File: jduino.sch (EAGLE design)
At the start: 20 parts, among them IC1 7805T, IC2 ATMEGA48/88/168-PU, Q1 16 mHz

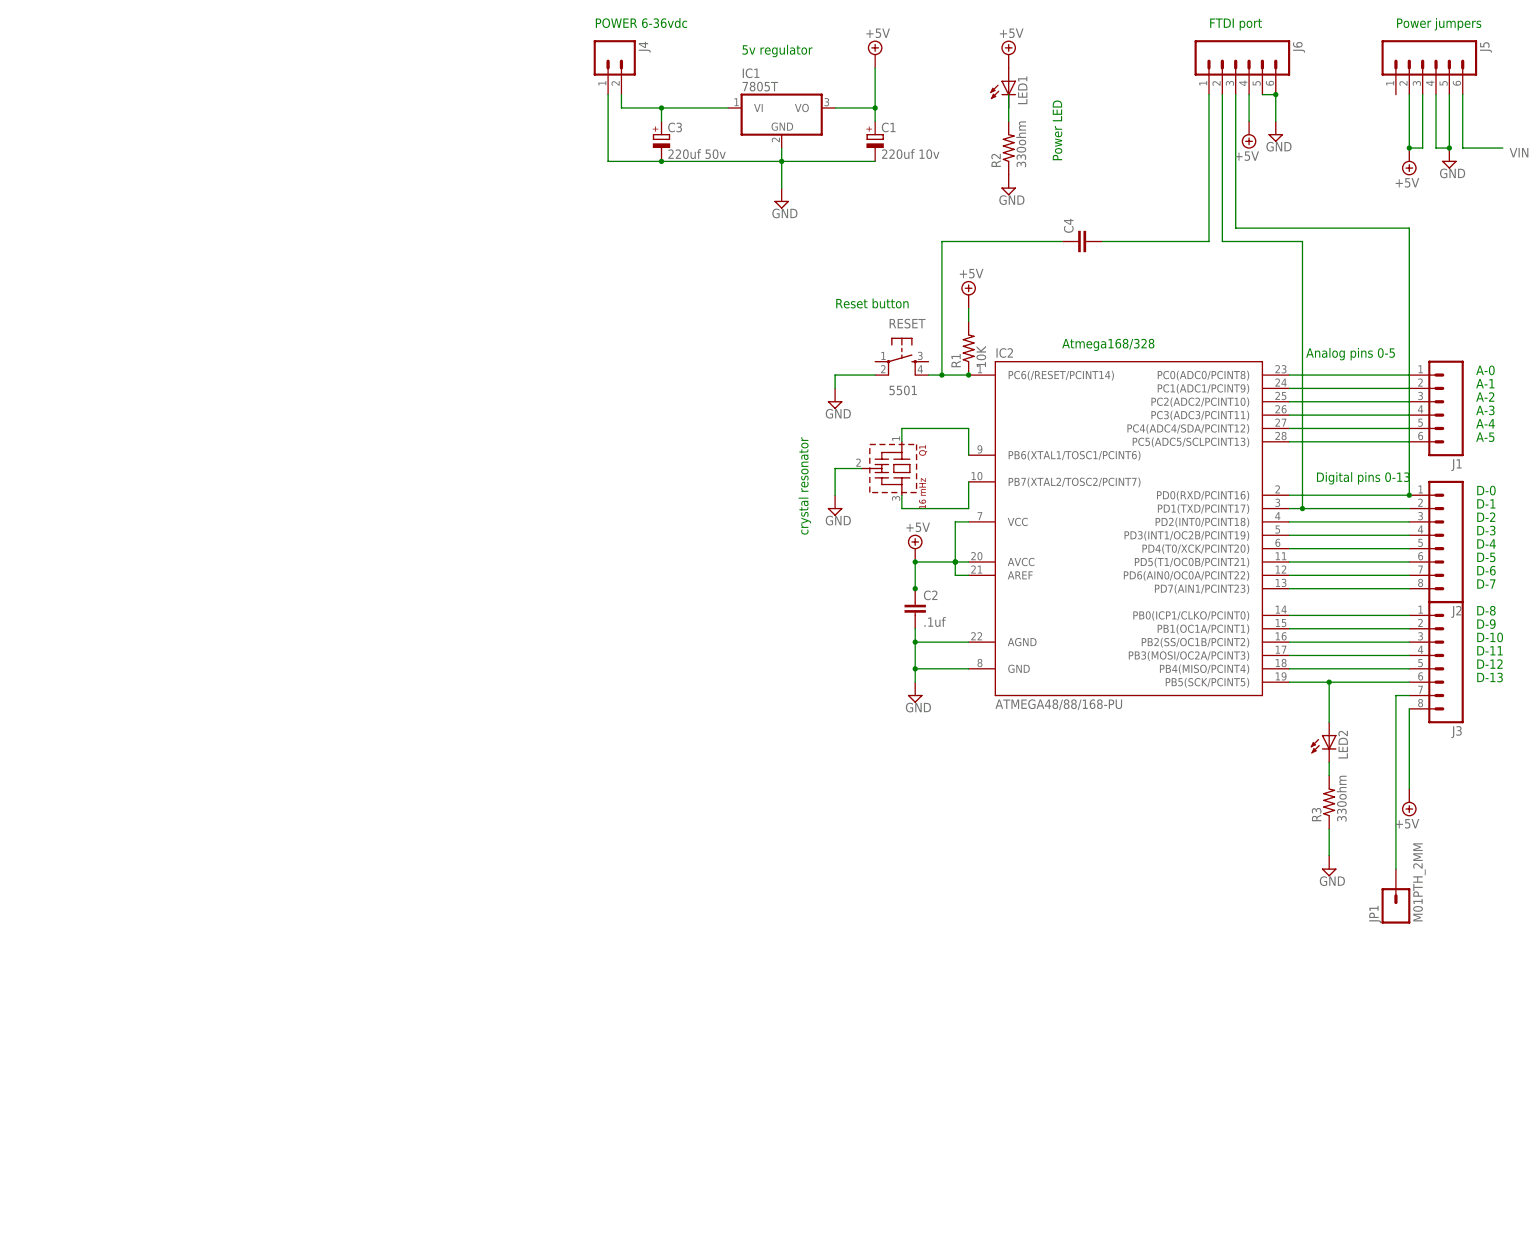
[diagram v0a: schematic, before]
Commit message: Added power elements.
Added a protection diode and a power switch. Also swapped out the
7805 for a LDO regulator.
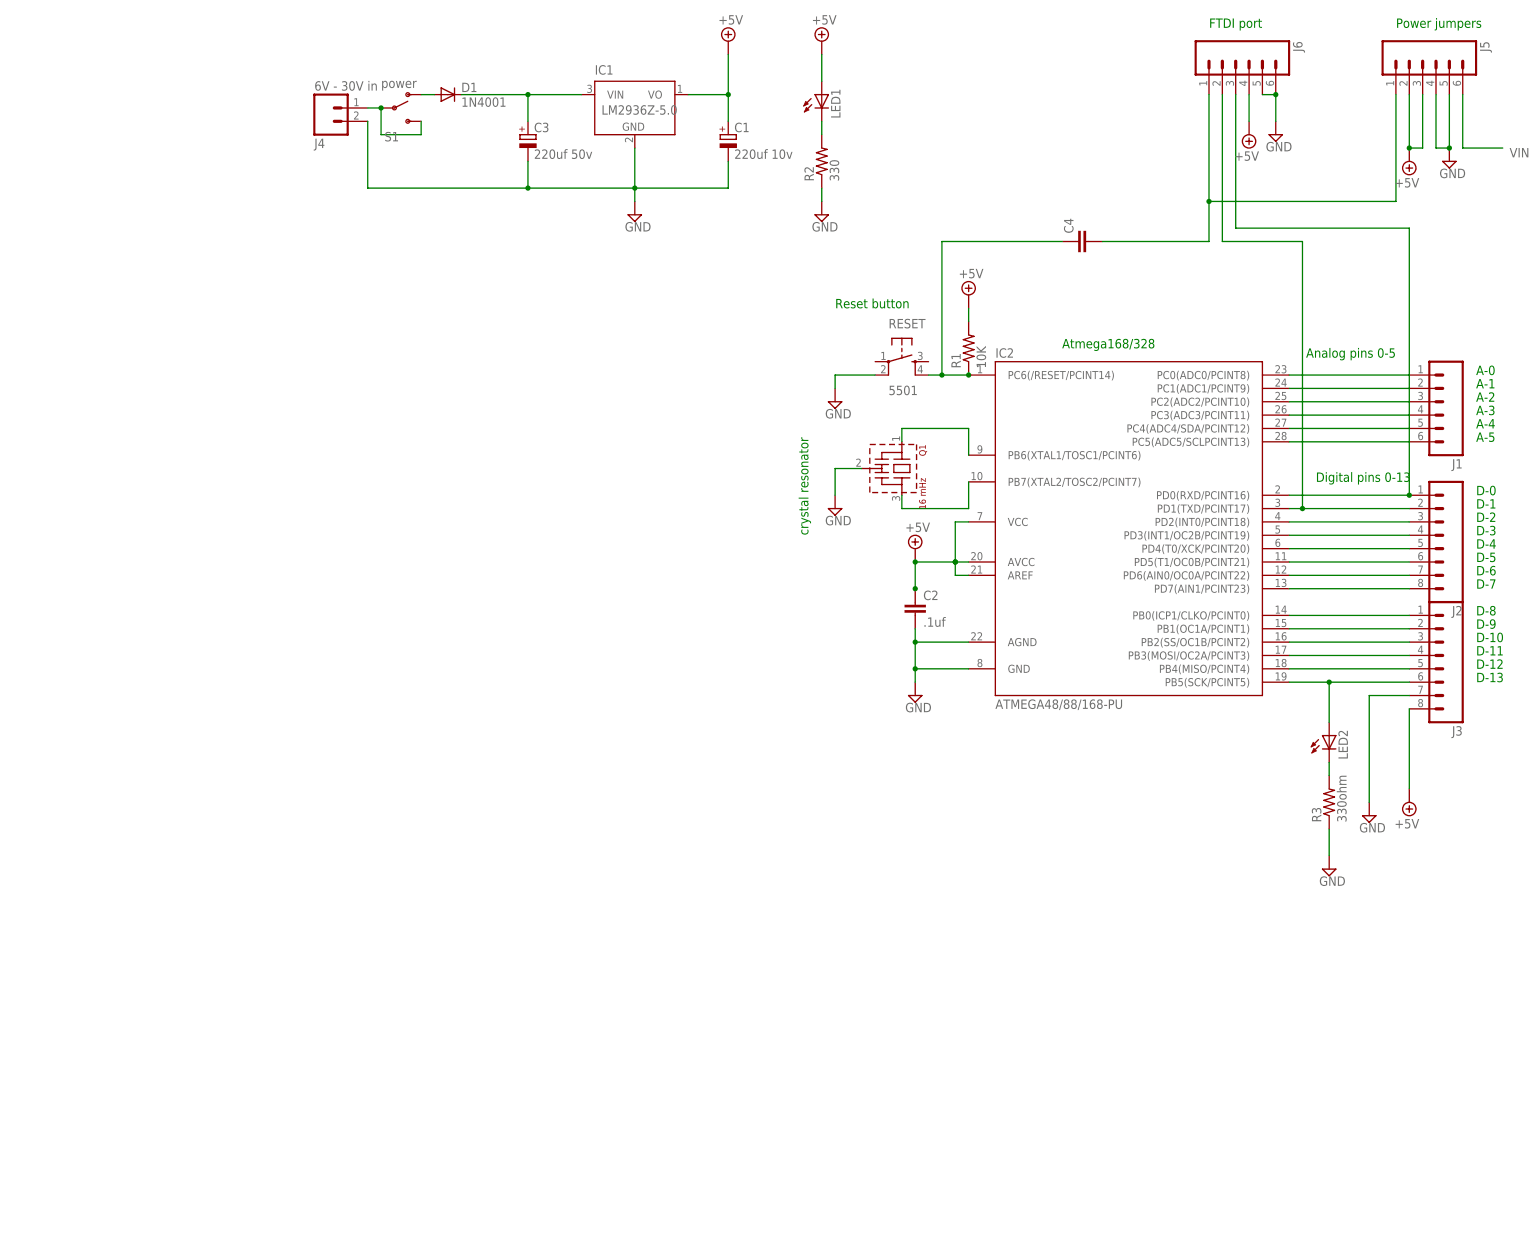
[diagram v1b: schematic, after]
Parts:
- removed JP1: M01PTH_2MM, SparkFun:M01PTH_2MM
- added D1: 1N4001, SparkFun-DiscreteSemi:DIODEPTH
- added S1: power, SparkFun-Electromechanical:SWITCH-SPDTPTH
- IC1: value 7805T -> LM2936Z-5.0; device linear:7805T -> national-semiconductor:LM2936Z-5.0
- J4: value (none) -> 6V - 30V in
- R2: value 330ohm -> 330
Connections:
- new net N$6: C3.+, D1.C, IC1.VIN
- new net N$7: D1.A, S1.O
- net GND: now also J3.7, J4.2; no longer J4.1
- net N$1: now also J5.1
- net N$2: now also J4.1, S1.P, S1.S; no longer J3.7, JP1.1
- net VIN: no longer C3.+, IC1.VI, J4.2
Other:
- note removed: "5v regulator"
- note removed: "POWER 6-36vdc"
- note removed: "Power LED"
- moved on the sheet: C1, C3, J4, LED1, R2

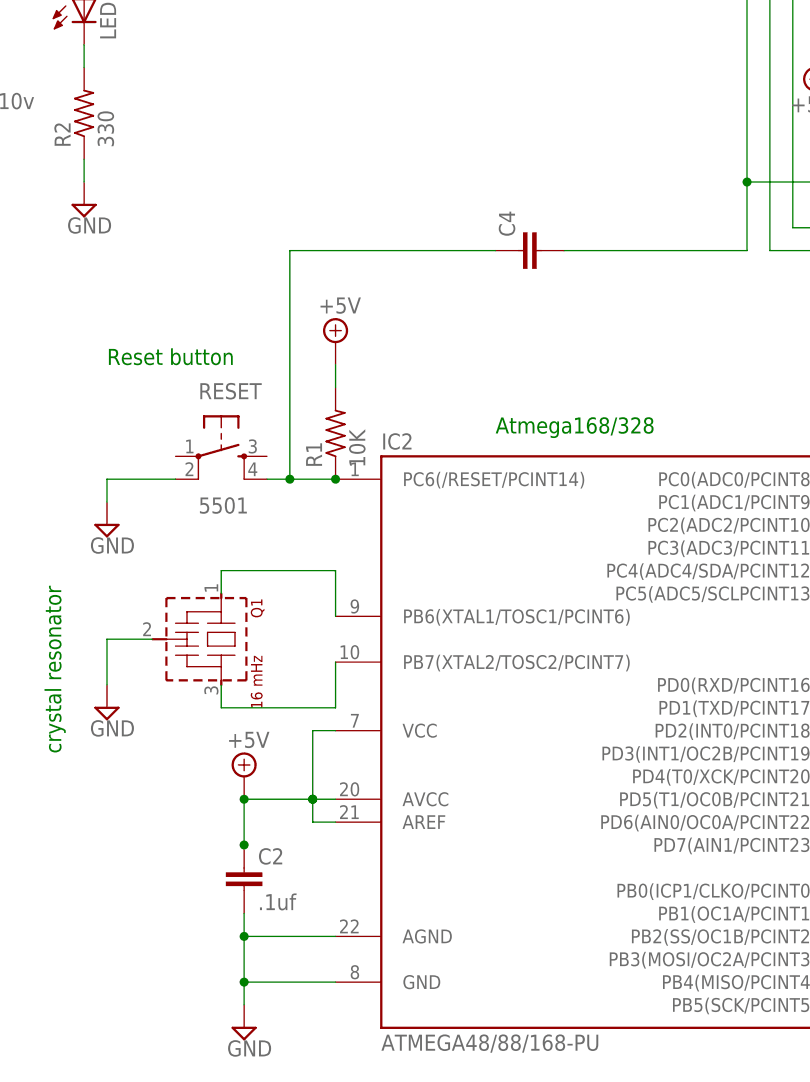
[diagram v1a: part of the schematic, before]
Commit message: Replaced Euro-stype capacitors.
Replaced the large reset capacitors with smaller-package 0.1 uF
capacitors.
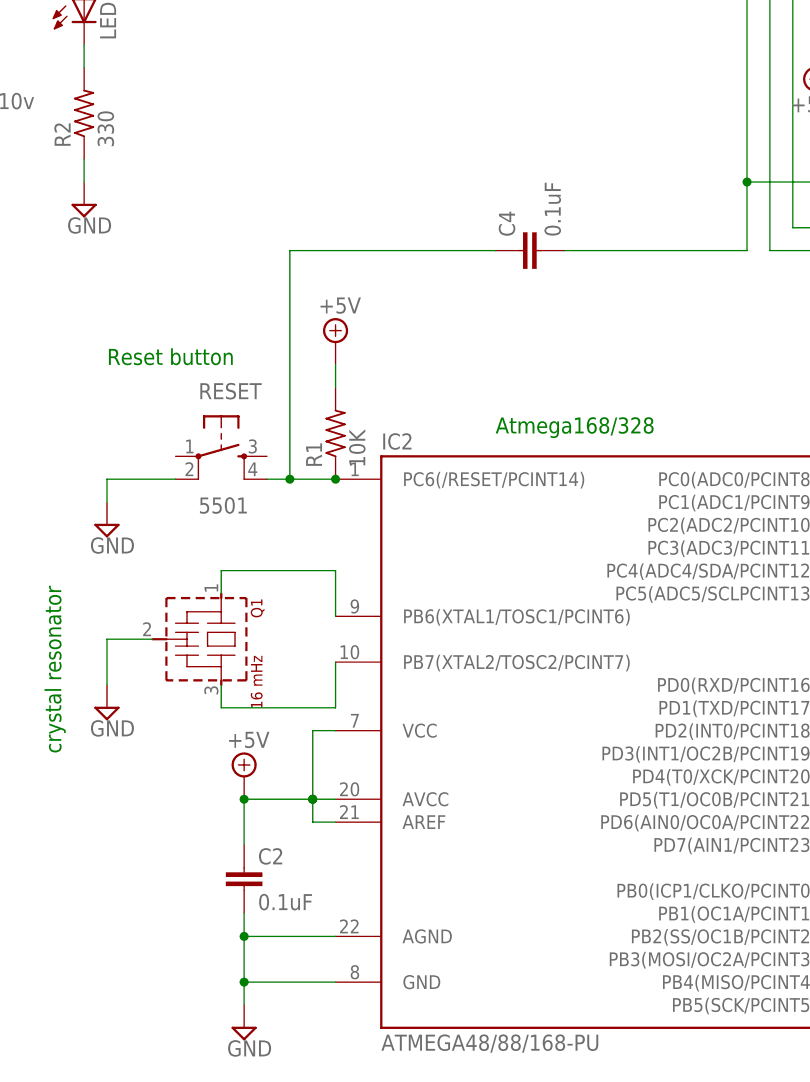
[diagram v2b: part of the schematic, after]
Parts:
- C2: value .1uf -> 0.1uF; device rcl:C-EU050-024X044 -> SparkFun-Passives:CAPPTH2
- C4: value (none) -> 0.1uF; device rcl:C-EU075-032X103 -> SparkFun-Passives:CAPPTH2
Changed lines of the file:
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@@
 </variantdefs>
 <classes>
-<class number="0" name="default" width="0.3048" drill="0.2032">
+<class number="0" name="default" width="0.4572" drill="0.2032">
 <clearance class="0" value="0.2032"/>
 </class>
-<class number="1" name="power" width="0.4064" drill="0.2032">
+<class number="1" name="power" width="0.6096" drill="0.2032">
 <clearance class="1" value="0.2032"/>
 </class>
@@
 <parts>
 <part name="C1" library="rcl" deviceset="CPOL-EU" device="E2.5-6" value="220uf 10v"/>
-<part name="C2" library="rcl" deviceset="C-EU" device="050-024X044" value=".1uf"/>
 <part name="IC2" library="atmega8" deviceset="ATMEGA48/88/168-PU" device=""/>
 <part name="SUPPLY2" library="supply2" deviceset="GND" device=""/>
@@
 <part name="SUPPLY12" library="supply2" deviceset="GND" device=""/>
 <part name="SUPPLY13" library="supply2" deviceset="+5V" device=""/>
-<part name="C4" library="rcl" deviceset="C-EU" device="075-032X103"/>
 <part name="SUPPLY14" library="supply2" deviceset="+5V" device=""/>
 <part name="LED2" library="led" deviceset="LED" device="3MM"/>
@@
 <part name="D1" library="SparkFun-DiscreteSemi" deviceset="DIODE" device="PTH" value="1N4001"/>
 <part name="IC1" library="national-semiconductor" deviceset="LM2936?*" device="Z" technology="-5.0"/>
+<part name="C2" library="SparkFun-Passives" deviceset="CAP" device="PTH2" value="0.1uF"/>
+<part name="C4" library="SparkFun-Passives" deviceset="CAP" device="PTH2" value="0.1uF"/>
 </parts>
 <sheets>
@@
 <attribute name="VALUE" x="18.923" y="117.3226" size="1.778" layer="96"/>
 </instance>
-<instance part="C2" gate="G$1" x="53.34" y="33.02"/>
 <instance part="IC2" gate="1" x="93.98" y="48.26"/>
 <instance part="SUPPLY2" gate="GND" x="0" y="106.68"/>
@@
 <instance part="SUPPLY12" gate="GND" x="121.92" y="121.92"/>
 <instance part="SUPPLY13" gate="+5V" x="116.84" y="121.92" rot="R180"/>
-<instance part="C4" gate="G$1" x="83.82" y="101.6" rot="R90"/>
 <instance part="SUPPLY14" gate="+5V" x="147.32" y="-5.08" rot="R180"/>
 <instance part="LED2" gate="G$1" x="132.08" y="7.62"/>
@@
 <instance part="D1" gate="G$1" x="-35.56" y="129.54"/>
 <instance part="IC1" gate="G$1" x="0" y="127"/>
+<instance part="C2" gate="G$1" x="53.34" y="30.48"/>
+<instance part="C4" gate="G$1" x="86.36" y="101.6" rot="R90"/>
 </instances>
 <busses>
@@
 <junction x="60.96" y="40.64"/>
 <junction x="60.96" y="40.64"/>
-<junction x="53.34" y="35.56"/>
 <junction x="53.34" y="40.64"/>
 <pinref part="IC2" gate="1" pin="AREF"/>
 <pinref part="IC2" gate="1" pin="AVCC"/>
 <pinref part="IC2" gate="1" pin="VCC@1"/>
+<pinref part="SUPPLY6" gate="+5V" pin="+5V"/>
 <pinref part="C2" gate="G$1" pin="1"/>
-<pinref part="SUPPLY6" gate="+5V" pin="+5V"/>
 </segment>
 <segment>
@@
 <wire x1="88.9" y1="101.6" x2="109.22" y2="101.6" width="0.1524" layer="91"/>
 <pinref part="J6" gate="G$1" pin="1"/>
-<pinref part="C4" gate="G$1" pin="2"/>
 <pinref part="J5" gate="G$1" pin="1"/>
 <wire x1="109.22" y1="109.22" x2="144.78" y2="109.22" width="0.1524" layer="91"/>
 <wire x1="144.78" y1="109.22" x2="144.78" y2="129.54" width="0.1524" layer="91"/>
 <junction x="109.22" y="109.22"/>
-</segment>
-</net>
+<pinref part="C4" gate="G$1" pin="2"/>
+</segment>
+</net>
